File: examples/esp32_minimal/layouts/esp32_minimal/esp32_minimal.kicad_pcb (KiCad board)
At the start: 2 copper layers, 36.2 x 26.8 mm, 20 parts

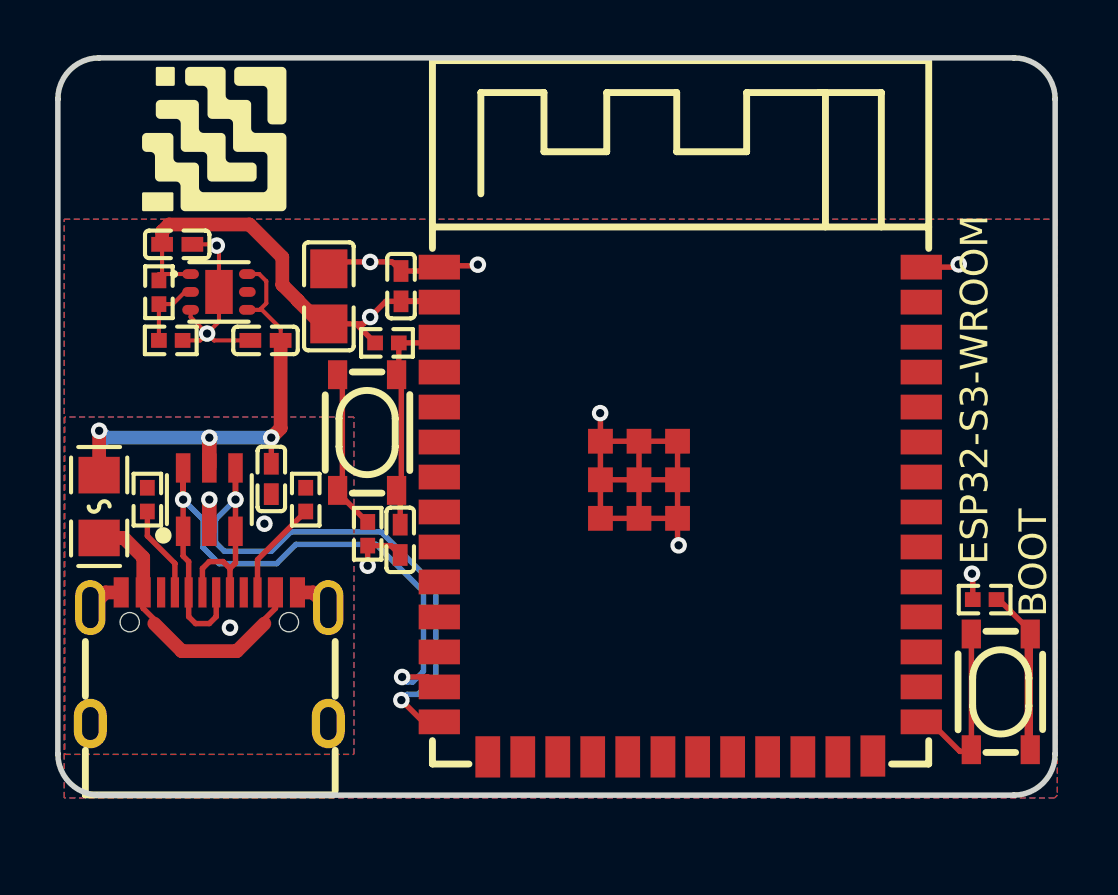
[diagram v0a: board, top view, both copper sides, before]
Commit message: revert node to main, fix all .is_unit references on unit instances
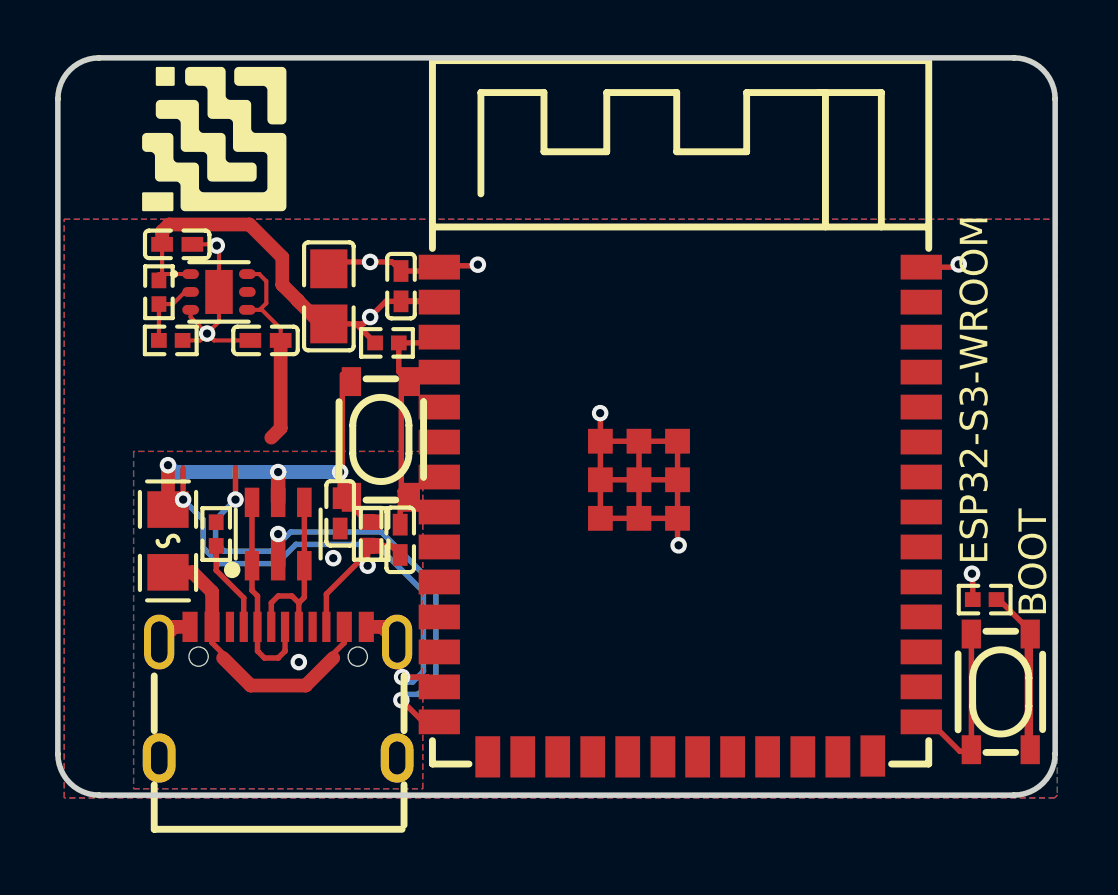
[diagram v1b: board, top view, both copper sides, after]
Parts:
- moved C3 2.80 mm to (139.5, 127.5)
- moved D1 2.80 mm to (137.2, 128.2)
- moved F1 2.80 mm to (133.2, 128.5)
- moved R6 2.80 mm to (135.0, 128.2)
- moved R7 2.80 mm to (140.8, 128.2)
- moved USB1 2.80 mm to (137.2, 134.0)
- moved SW2 0.56 mm to (141.0, 124.8)

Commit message: bug fix
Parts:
- moved SW2 0.56 mm to (141.5, 125.1)
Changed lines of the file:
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@@
 	(footprint "ALPSALPINE_SKRPACE010:KEY-SMD_4P-L4.2-W3.2-P2.20-LS4.6"
 		(layer "F.Cu")
-		(at 140.978656 124.815054 90)
+		(at 141.478656 125.065054 90)
 		(property "Reference" "SW2"
 			(at 0 -5.07 90)

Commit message: pytest fixes
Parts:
- moved C3 0.56 mm to (140.0, 127.8)
- moved D1 0.56 mm to (137.8, 128.5)
- moved F1 0.56 mm to (133.8, 128.8)
- moved R6 0.56 mm to (135.5, 128.5)
- moved R7 0.56 mm to (141.2, 128.5)
- moved USB1 0.56 mm to (137.8, 134.2)

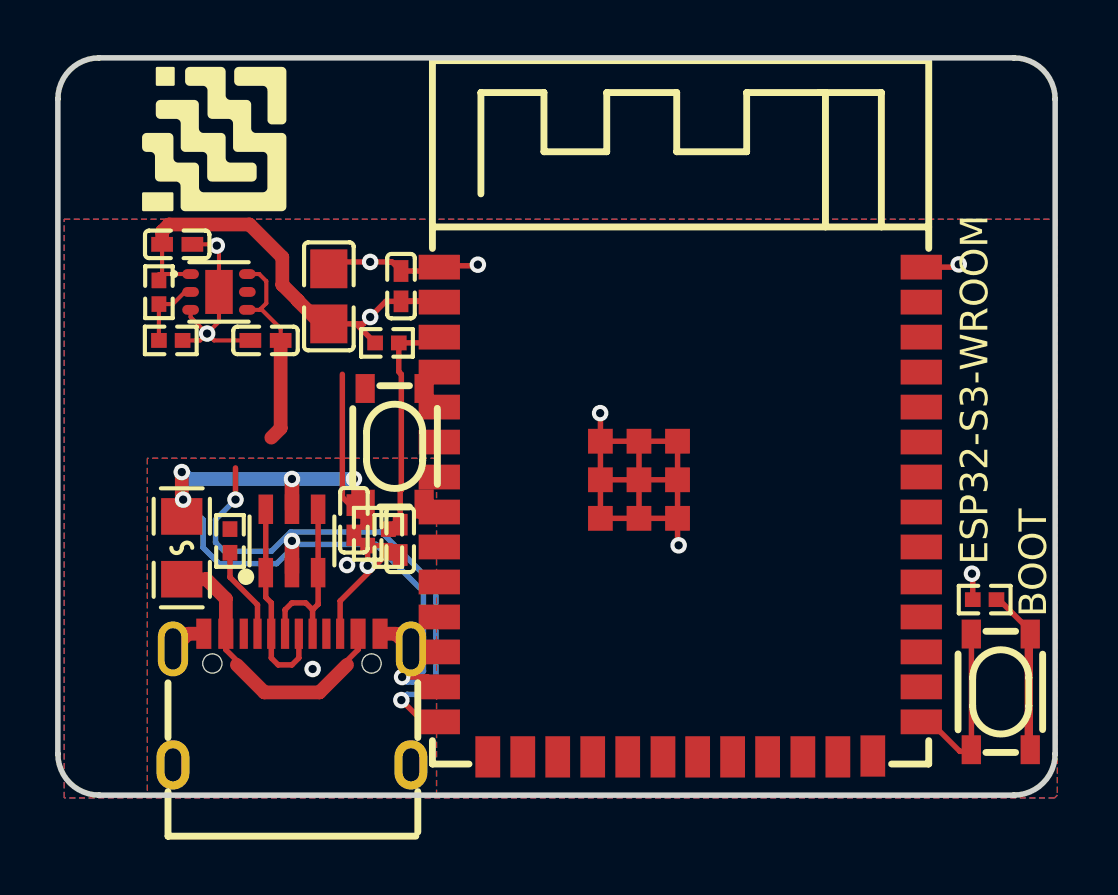
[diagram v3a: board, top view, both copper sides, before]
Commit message: revert esp32minimal changes to main
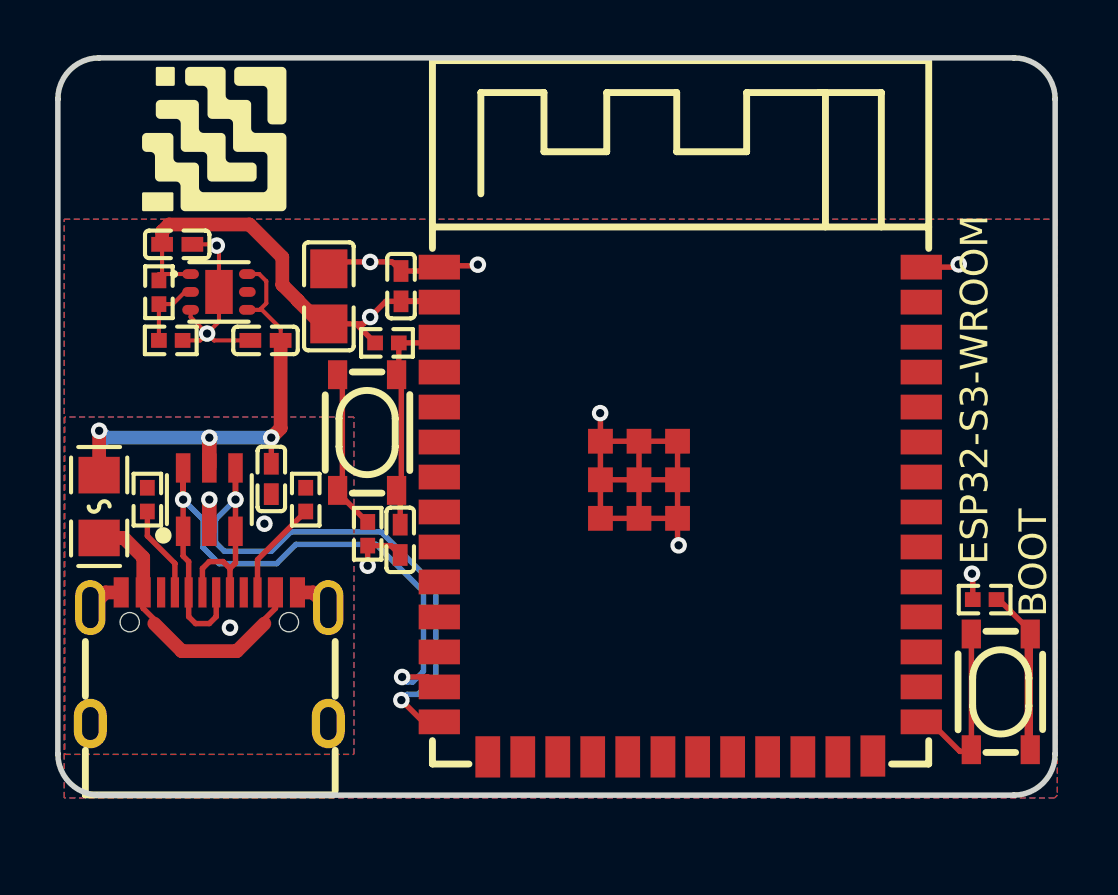
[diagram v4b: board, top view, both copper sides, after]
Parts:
- moved C3 3.35 mm to (137.0, 126.2)
- moved D1 3.35 mm to (134.8, 127.0)
- moved F1 3.35 mm to (130.8, 127.2)
- moved R6 3.35 mm to (132.5, 127.0)
- moved R7 3.35 mm to (138.2, 127.0)
- moved USB1 3.35 mm to (134.8, 132.8)
- moved SW2 1.12 mm to (140.5, 124.6)
